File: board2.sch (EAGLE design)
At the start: 79 parts, among them Q1 7.68MHz, Q2 16MHz

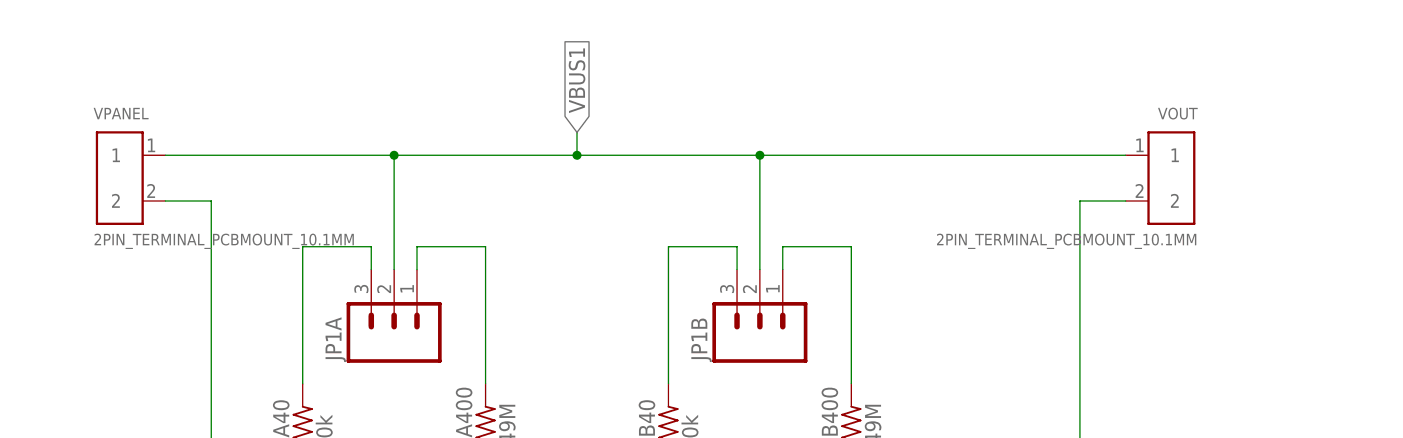
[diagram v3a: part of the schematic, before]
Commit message: IMPORTANT: Changed the terminals for the PV connectors. They are bigger and with double connections
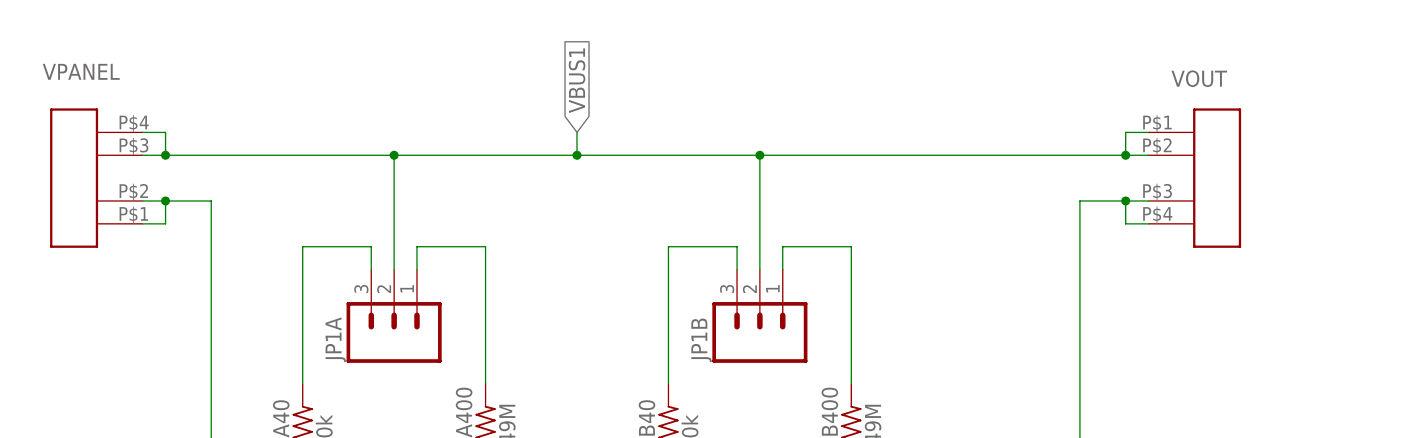
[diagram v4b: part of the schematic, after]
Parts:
- VOUT, VPANEL: value 2PIN_TERMINAL_PCBMOUNT_10.1MM -> PAS-PHOENIXTERMINAL2PIN-10.16MM; device TE CONNECTIVITY:2PIN_TERMINAL_PCBMOUNT_10.1MM -> PAS-PHOENIXTERMINAL:PAS-PHOENIXTERMINAL2PIN-10.16MM
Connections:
- net AIN3: now also VOUT.P$3, VOUT.P$4; no longer VOUT.2
- net VBUS1: now also VOUT.P$1, VOUT.P$2, VPANEL.P$3, VPANEL.P$4; no longer VOUT.1, VPANEL.1
- net VBUS2: now also VPANEL.P$1, VPANEL.P$2; no longer VPANEL.2
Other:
- note added: "Measuring PCB v2.5"
- note removed: "Measuring PCB v2.4"
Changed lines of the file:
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@@
 </classes>
 <parts>
-<part name="VPANEL" library="TE CONNECTIVITY" deviceset="2PIN_TERMINAL_PCBMOUNT_10.1MM" device=""/>
-<part name="VOUT" library="TE CONNECTIVITY" deviceset="2PIN_TERMINAL_PCBMOUNT_10.1MM" device=""/>
 <part name="JP1A" library="SparkFun-Connectors" deviceset="M03" device="PTH"/>
 <part name="JP1B" library="SparkFun-Connectors" deviceset="M03" device="PTH"/>
@@
 <part name="D0-D3" library="SparkFun-Connectors" deviceset="M04" device="NO_SILK_ALL_ROUND"/>
 <part name="C35" library="adafruit" deviceset="C-US" device="C3216" value="1u"/>
+<part name="VPANEL" library="PAS-PHOENIXTERMINAL" deviceset="PAS-PHOENIXTERMINAL2PIN-10.16MM" device=""/>
+<part name="VOUT" library="PAS-PHOENIXTERMINAL" deviceset="PAS-PHOENIXTERMINAL2PIN-10.16MM" device=""/>
 </parts>
 <sheets>
@@
 <text x="-5.08" y="-175.26" size="5.08" layer="98">Standalone Arduino (atmega328)</text>
 <text x="322.58" y="-175.26" size="5.08" layer="98">Connectors</text>
-<text x="381" y="-228.6" size="6.4516" layer="98">Measuring PCB v2.4</text>
+<text x="381" y="-228.6" size="6.4516" layer="98">Measuring PCB v2.5</text>
 <wire x1="370.84" y1="-281.94" x2="370.84" y2="-248.92" width="0.1524" layer="98"/>
 <wire x1="370.84" y1="-248.92" x2="370.84" y2="-233.68" width="0.1524" layer="98"/>
@@
 </plain>
 <instances>
-<instance part="VPANEL" gate="G$1" x="12.7" y="48.26"/>
-<instance part="VOUT" gate="G$1" x="119.38" y="48.26" rot="MR0"/>
 <instance part="JP1A" gate="G$1" x="38.1" y="27.94" rot="R90"/>
 <instance part="JP1B" gate="G$1" x="78.74" y="27.94" rot="R90"/>
@@
 <instance part="D0-D3" gate="G$1" x="350.52" y="-256.54" rot="R180"/>
 <instance part="C35" gate="G$1" x="170.18" y="-129.54"/>
+<instance part="VPANEL" gate="G$1" x="2.54" y="43.18" smashed="yes" rot="R180">
+<attribute name="NAME" x="7.62" y="58.42" size="1.778" layer="95" rot="R180"/>
+</instance>
+<instance part="VOUT" gate="G$1" x="129.54" y="48.26" smashed="yes">
+<attribute name="NAME" x="124.46" y="55.88" size="1.778" layer="95"/>
+</instance>
 </instances>
 <busses>
@@
 <net name="VBUS1" class="0">
 <segment>
-<pinref part="VPANEL" gate="G$1" pin="1"/>
-<pinref part="VOUT" gate="G$1" pin="1"/>
+<wire x1="10.16" y1="48.26" x2="12.7" y2="48.26" width="0.1524" layer="91"/>
+<pinref part="JP1A" gate="G$1" pin="2"/>
 <wire x1="12.7" y1="48.26" x2="38.1" y2="48.26" width="0.1524" layer="91"/>
-<pinref part="JP1A" gate="G$1" pin="2"/>
 <wire x1="38.1" y1="48.26" x2="58.42" y2="48.26" width="0.1524" layer="91"/>
 <wire x1="58.42" y1="48.26" x2="78.74" y2="48.26" width="0.1524" layer="91"/>
 <wire x1="78.74" y1="48.26" x2="119.38" y2="48.26" width="0.1524" layer="91"/>
+<wire x1="119.38" y1="48.26" x2="121.92" y2="48.26" width="0.1524" layer="91"/>
 <wire x1="38.1" y1="35.56" x2="38.1" y2="48.26" width="0.1524" layer="91"/>
 <junction x="38.1" y="48.26"/>
@@
 <junction x="58.42" y="48.26"/>
 <label x="58.42" y="50.8" size="1.778" layer="95" rot="R90" xref="yes"/>
+<pinref part="VPANEL" gate="G$1" pin="P$3"/>
+<pinref part="VPANEL" gate="G$1" pin="P$4"/>
+<wire x1="10.16" y1="50.8" x2="12.7" y2="50.8" width="0.1524" layer="91"/>
+<wire x1="12.7" y1="50.8" x2="12.7" y2="48.26" width="0.1524" layer="91"/>
+<junction x="12.7" y="48.26"/>
+<pinref part="VOUT" gate="G$1" pin="P$2"/>
+<wire x1="119.38" y1="48.26" x2="119.38" y2="50.8" width="0.1524" layer="91"/>
+<junction x="119.38" y="48.26"/>
+<pinref part="VOUT" gate="G$1" pin="P$1"/>
+<wire x1="119.38" y1="50.8" x2="121.92" y2="50.8" width="0.1524" layer="91"/>
 </segment>
 </net>
@@
 <net name="AIN3" class="0">
 <segment>
-<pinref part="VOUT" gate="G$1" pin="2"/>
+<wire x1="121.92" y1="43.18" x2="119.38" y2="43.18" width="0.1524" layer="91"/>
 <wire x1="119.38" y1="43.18" x2="114.3" y2="43.18" width="0.1524" layer="91"/>
 <wire x1="114.3" y1="43.18" x2="114.3" y2="-35.56" width="0.1524" layer="91"/>
@@
 <junction x="86.36" y="-25.4"/>
 <label x="99.06" y="-25.4" size="1.778" layer="95" xref="yes"/>
+<pinref part="VOUT" gate="G$1" pin="P$3"/>
+<pinref part="VOUT" gate="G$1" pin="P$4"/>
+<wire x1="121.92" y1="40.64" x2="119.38" y2="40.64" width="0.1524" layer="91"/>
+<wire x1="119.38" y1="40.64" x2="119.38" y2="43.18" width="0.1524" layer="91"/>
+<junction x="119.38" y="43.18"/>
 </segment>
 <segment>
@@
 <wire x1="22.86" y1="-35.56" x2="17.78" y2="-35.56" width="0.1524" layer="91"/>
 <wire x1="17.78" y1="-35.56" x2="17.78" y2="2.54" width="0.1524" layer="91"/>
-<pinref part="VPANEL" gate="G$1" pin="2"/>
 <wire x1="17.78" y1="2.54" x2="17.78" y2="43.18" width="0.1524" layer="91"/>
 <wire x1="17.78" y1="43.18" x2="12.7" y2="43.18" width="0.1524" layer="91"/>
+<wire x1="12.7" y1="43.18" x2="10.16" y2="43.18" width="0.1524" layer="91"/>
 <wire x1="17.78" y1="2.54" x2="15.24" y2="2.54" width="0.1524" layer="91"/>
 <junction x="17.78" y="2.54"/>
@@
 <wire x1="25.4" y1="-35.56" x2="22.86" y2="-35.56" width="0.1524" layer="91"/>
 <junction x="22.86" y="-35.56"/>
-</segment>
-</net>
+<pinref part="VPANEL" gate="G$1" pin="P$2"/>
+<pinref part="VPANEL" gate="G$1" pin="P$1"/>
+<wire x1="10.16" y1="40.64" x2="12.7" y2="40.64" width="0.1524" layer="91"/>
+<wire x1="12.7" y1="40.64" x2="12.7" y2="43.18" width="0.1524" layer="91"/>
+<junction x="12.7" y="43.18"/>
+</segment>
+</net>

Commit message: Updated connectors and schematic. No big changes
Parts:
- RESET: value TAC_SWITCHSMD -> SWITCH-MOMENTARY-2SMD-4; device SparkFun-Retired:TAC_SWITCHSMD -> SparkFun-Electromechanical:SWITCH-MOMENTARY-2SMD-4
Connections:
- net GND_ISO: no longer RESET.2
- net RESET: now also RESET.2; no longer RESET.3, RESET.4
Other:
- note added: "April 2016"
- note added: "Measuring PCB v2.6"
- note removed: "March 2016"
- note removed: "Measuring PCB v2.5"
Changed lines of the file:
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@@
 <part name="DS3234" library="SparkFun-FreqCtrl" deviceset="DS3234" device=""/>
 <part name="ICSP" library="SparkFun-Connectors" deviceset="M03X2" device="FEMALE" value="FEMALE 2x3"/>
-<part name="RESET" library="SparkFun-Retired" deviceset="TAC_SWITCH" device="SMD" value="TAC_SWITCHSMD"/>
 <part name="ADUM5000" library="Analog Devices_By_element14_Batch_1" deviceset="ADUM5000ARWZ" device=""/>
 <part name="MAX14850" library="MAX14850ASE" deviceset="IC_DIL16" device="-SOIC-16"/>
@@
 <part name="VPANEL" library="PAS-PHOENIXTERMINAL" deviceset="PAS-PHOENIXTERMINAL2PIN-10.16MM" device=""/>
 <part name="VOUT" library="PAS-PHOENIXTERMINAL" deviceset="PAS-PHOENIXTERMINAL2PIN-10.16MM" device=""/>
+<part name="RESET" library="SparkFun-Electromechanical" deviceset="SWITCH-MOMENTARY-2" device="SMD-4"/>
 </parts>
 <sheets>
@@
 <text x="-5.08" y="-175.26" size="5.08" layer="98">Standalone Arduino (atmega328)</text>
 <text x="322.58" y="-175.26" size="5.08" layer="98">Connectors</text>
-<text x="381" y="-228.6" size="6.4516" layer="98">Measuring PCB v2.5</text>
+<text x="381" y="-228.6" size="6.4516" layer="98">Measuring PCB v2.6</text>
 <wire x1="370.84" y1="-281.94" x2="370.84" y2="-248.92" width="0.1524" layer="98"/>
 <wire x1="370.84" y1="-248.92" x2="370.84" y2="-233.68" width="0.1524" layer="98"/>
@@
 <wire x1="439.42" y1="-233.68" x2="439.42" y2="-248.92" width="0.1524" layer="98"/>
 <text x="441.96" y="-238.76" size="2.54" layer="98">date</text>
-<text x="462.28" y="-246.38" size="5.08" layer="98">March 2016</text>
+<text x="462.28" y="-246.38" size="5.08" layer="98">April 2016</text>
 <text x="373.38" y="-254" size="2.54" layer="98">description</text>
 <text x="378.46" y="-279.4" size="3.302" layer="98">This board measures Voltage, Current and Temperature of a PV
@@
 <instance part="DS3234" gate="G$1" x="88.9" y="-127"/>
 <instance part="ICSP" gate="G$1" x="411.48" y="-187.96"/>
-<instance part="RESET" gate="S" x="139.7" y="-187.96"/>
 <instance part="ADUM5000" gate="A" x="411.48" y="22.86"/>
 <instance part="MAX14850" gate="IC" x="411.48" y="-43.18"/>
@@
 <attribute name="NAME" x="124.46" y="55.88" size="1.778" layer="95"/>
 </instance>
+<instance part="RESET" gate="G$1" x="137.16" y="-187.96"/>
 </instances>
 <busses>
@@
 </segment>
 <segment>
-<pinref part="RESET" gate="S" pin="2"/>
-<wire x1="134.62" y1="-190.5" x2="132.08" y2="-190.5" width="0.1524" layer="91"/>
-<wire x1="132.08" y1="-190.5" x2="132.08" y2="-187.96" width="0.1524" layer="91"/>
-<pinref part="RESET" gate="S" pin="1"/>
-<wire x1="134.62" y1="-187.96" x2="132.08" y2="-187.96" width="0.1524" layer="91"/>
 <wire x1="132.08" y1="-187.96" x2="127" y2="-187.96" width="0.1524" layer="91"/>
-<junction x="132.08" y="-187.96"/>
 <label x="127" y="-187.96" size="1.778" layer="95" rot="R180" xref="yes"/>
+<pinref part="RESET" gate="G$1" pin="1"/>
 </segment>
 <segment>
@@
 <pinref part="ATMEGA328" gate="U$1" pin="PC6(/RESET)"/>
 <wire x1="142.24" y1="-203.2" x2="147.32" y2="-203.2" width="0.1524" layer="91"/>
-<pinref part="RESET" gate="S" pin="3"/>
 <wire x1="147.32" y1="-203.2" x2="149.86" y2="-203.2" width="0.1524" layer="91"/>
 <wire x1="149.86" y1="-203.2" x2="152.4" y2="-203.2" width="0.1524" layer="91"/>
-<wire x1="144.78" y1="-187.96" x2="147.32" y2="-187.96" width="0.1524" layer="91"/>
-<wire x1="147.32" y1="-187.96" x2="147.32" y2="-190.5" width="0.1524" layer="91"/>
 <junction x="147.32" y="-203.2"/>
-<pinref part="RESET" gate="S" pin="4"/>
-<wire x1="147.32" y1="-190.5" x2="147.32" y2="-203.2" width="0.1524" layer="91"/>
-<wire x1="144.78" y1="-190.5" x2="147.32" y2="-190.5" width="0.1524" layer="91"/>
-<junction x="147.32" y="-190.5"/>
+<wire x1="147.32" y1="-187.96" x2="147.32" y2="-203.2" width="0.1524" layer="91"/>
 <wire x1="149.86" y1="-203.2" x2="149.86" y2="-185.42" width="0.1524" layer="91"/>
 <junction x="149.86" y="-203.2"/>
 <wire x1="149.86" y1="-185.42" x2="160.02" y2="-185.42" width="0.1524" layer="91"/>
 <label x="160.02" y="-185.42" size="1.778" layer="95" xref="yes"/>
-</segment>
-<segment>
+<pinref part="RESET" gate="G$1" pin="2"/>
+<wire x1="147.32" y1="-187.96" x2="142.24" y2="-187.96" width="0.1524" layer="91"/>
+</segment>
+<segment>

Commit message: Small changes
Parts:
- added LED1: (no value), adafruit:LEDCHIPLED_0805
- added R12: 1k, adafruit:R-US_R3216
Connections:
- new net N$18: ATMEGA328.PC1(ADC1), R12.1
- new net N$19: LED1.A, R12.2
- net GND_ISO: now also LED1.C
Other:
- note added: "Measuring PCB v2.7"
- note removed: "Measuring PCB v2.6"
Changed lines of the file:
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@@
 <part name="VOUT" library="PAS-PHOENIXTERMINAL" deviceset="PAS-PHOENIXTERMINAL2PIN-10.16MM" device=""/>
 <part name="RESET" library="SparkFun-Electromechanical" deviceset="SWITCH-MOMENTARY-2" device="SMD-4"/>
+<part name="R12" library="adafruit" deviceset="R-US_" device="R3216" value="1k"/>
+<part name="LED1" library="adafruit" deviceset="LED" device="CHIPLED_0805"/>
 </parts>
 <sheets>
@@
 <text x="-5.08" y="-175.26" size="5.08" layer="98">Standalone Arduino (atmega328)</text>
 <text x="322.58" y="-175.26" size="5.08" layer="98">Connectors</text>
-<text x="381" y="-228.6" size="6.4516" layer="98">Measuring PCB v2.6</text>
+<text x="381" y="-228.6" size="6.4516" layer="98">Measuring PCB v2.7</text>
 <wire x1="370.84" y1="-281.94" x2="370.84" y2="-248.92" width="0.1524" layer="98"/>
 <wire x1="370.84" y1="-248.92" x2="370.84" y2="-233.68" width="0.1524" layer="98"/>
@@
 </instance>
 <instance part="RESET" gate="G$1" x="137.16" y="-187.96"/>
+<instance part="R12" gate="G$1" x="213.36" y="-205.74"/>
+<instance part="LED1" gate="G$1" x="231.14" y="-205.74" rot="R90"/>
 </instances>
 <busses>
@@
 <label x="421.64" y="-190.5" size="1.778" layer="95" xref="yes"/>
 </segment>
+<segment>
+<pinref part="LED1" gate="G$1" pin="C"/>
+<wire x1="236.22" y1="-205.74" x2="241.3" y2="-205.74" width="0.1524" layer="91"/>
+<label x="241.3" y="-205.74" size="1.778" layer="95" xref="yes"/>
+</segment>
 </net>
 <net name="IN2_ISO" class="0">
@@
 <segment>
 <pinref part="ATMEGA328" gate="U$1" pin="PB2(SS/OC1B)"/>
-<wire x1="200.66" y1="-254" x2="233.68" y2="-254" width="0.1524" layer="91"/>
-<label x="233.68" y="-254" size="1.778" layer="95" xref="yes"/>
+<wire x1="200.66" y1="-254" x2="218.44" y2="-254" width="0.1524" layer="91"/>
+<label x="218.44" y="-254" size="1.778" layer="95" xref="yes"/>
 </segment>
 <segment>
@@
 </segment>
 </net>
+<net name="N$19" class="0">
+<segment>
+<pinref part="R12" gate="G$1" pin="2"/>
+<pinref part="LED1" gate="G$1" pin="A"/>
+<wire x1="228.6" y1="-205.74" x2="218.44" y2="-205.74" width="0.1524" layer="91"/>
+</segment>
+</net>
+<net name="N$18" class="0">
+<segment>
+<pinref part="R12" gate="G$1" pin="1"/>
+<pinref part="ATMEGA328" gate="U$1" pin="PC1(ADC1)"/>
+<wire x1="208.28" y1="-205.74" x2="200.66" y2="-205.74" width="0.1524" layer="91"/>
+</segment>
+</net>

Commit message: FINAL BOARD AS ORDERED - v2.7
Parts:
- renumbered SJ1-RST to RST, SJ2-SYNC to SYNC
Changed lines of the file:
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@@
 <part name="AIN6-7" library="SparkFun-Connectors" deviceset="M02" device="1X02_NO_SILK"/>
 <part name="ADS1256" library="Texas Instruments_By_element14_Batch_1" deviceset="ADS1256IDBT" device=""/>
-<part name="SJ1-RST" library="jumper" deviceset="SJ" device=""/>
-<part name="SJ2-SYNC" library="jumper" deviceset="SJ" device=""/>
+<part name="RST" library="jumper" deviceset="SJ" device=""/>
+<part name="SYNC" library="jumper" deviceset="SJ" device=""/>
 <part name="ATMEGA328" library="SparkFun-DigitalIC" deviceset="ATMEGA328P_TQFP" device="" value="ATMEGA328P_TQFP"/>
 <part name="DS3234" library="SparkFun-FreqCtrl" deviceset="DS3234" device=""/>
@@
 <instance part="AIN6-7" gate="G$1" x="353.06" y="-236.22" rot="R180"/>
 <instance part="ADS1256" gate="A" x="259.08" y="-10.16"/>
-<instance part="SJ1-RST" gate="1" x="198.12" y="-7.62"/>
-<instance part="SJ2-SYNC" gate="1" x="203.2" y="-12.7"/>
+<instance part="RST" gate="1" x="198.12" y="-7.62"/>
+<instance part="SYNC" gate="1" x="203.2" y="-12.7"/>
 <instance part="ATMEGA328" gate="U$1" x="177.8" y="-233.68"/>
 <instance part="DS3234" gate="G$1" x="88.9" y="-127"/>
@@
 <wire x1="190.5" y1="-10.16" x2="187.96" y2="-10.16" width="0.1524" layer="91"/>
 <label x="187.96" y="-10.16" size="1.778" layer="95" rot="R180" xref="yes"/>
-<pinref part="SJ1-RST" gate="1" pin="1"/>
+<pinref part="RST" gate="1" pin="1"/>
 <wire x1="190.5" y1="-10.16" x2="190.5" y2="-7.62" width="0.1524" layer="91"/>
 <wire x1="190.5" y1="-7.62" x2="193.04" y2="-7.62" width="0.1524" layer="91"/>
-<pinref part="SJ2-SYNC" gate="1" pin="1"/>
+<pinref part="SYNC" gate="1" pin="1"/>
 <wire x1="190.5" y1="-10.16" x2="190.5" y2="-12.7" width="0.1524" layer="91"/>
 <wire x1="190.5" y1="-12.7" x2="198.12" y2="-12.7" width="0.1524" layer="91"/>
@@
 <net name="N$17" class="0">
 <segment>
-<pinref part="SJ1-RST" gate="1" pin="2"/>
+<pinref part="RST" gate="1" pin="2"/>
 <pinref part="ADS1256" gate="A" pin="~RESET"/>
 <wire x1="203.2" y1="-7.62" x2="238.76" y2="-7.62" width="0.1524" layer="91"/>
@@
 <net name="N$20" class="0">
 <segment>
-<pinref part="SJ2-SYNC" gate="1" pin="2"/>
+<pinref part="SYNC" gate="1" pin="2"/>
 <pinref part="ADS1256" gate="A" pin="~SYNC,_~PDWN"/>
 <wire x1="208.28" y1="-12.7" x2="238.76" y2="-12.7" width="0.1524" layer="91"/>
